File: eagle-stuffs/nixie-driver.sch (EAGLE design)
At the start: 65 parts, among them IC1 74141N/K155ID1, IC2 74LS595N, IC4 NE555, Q1 MPSA92, Q10 2N2222, Q11 IRF840, Q12 2N2222, Q2 MPSA92, Q3 MPSA92, Q4 MPSA92, Q5 MPSA42, Q6 MPSA42, Q7 MPSA42, Q8 MPSA42, Q9 PN2907, U1 MC34063DIP

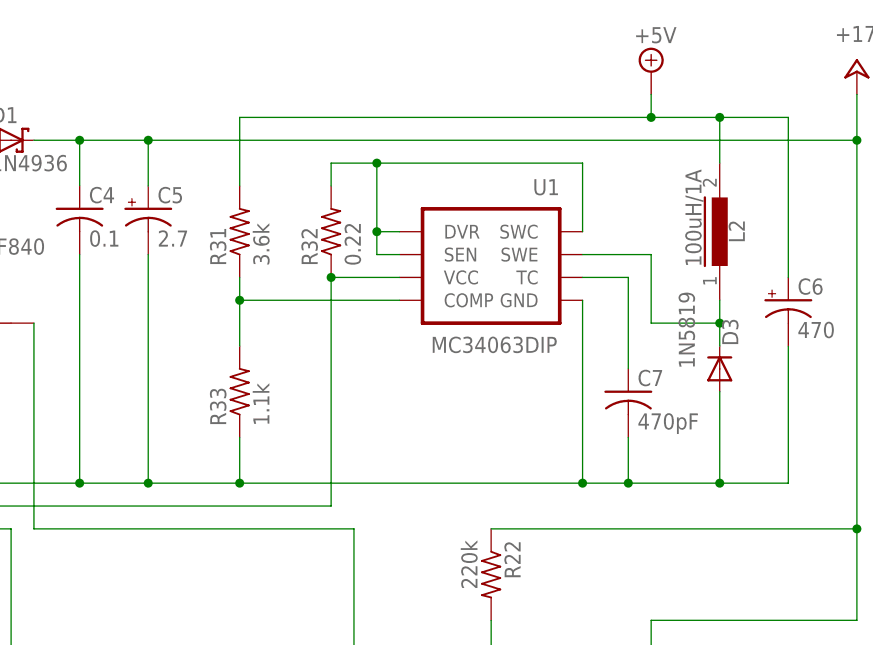
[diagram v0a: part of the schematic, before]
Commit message: Change fixed resistors for voltage output ajust. to pot.
The PI seems to be quite touchy about the voltage drop under load. Got
to push it to 5.1v to make the red led stop to blink!
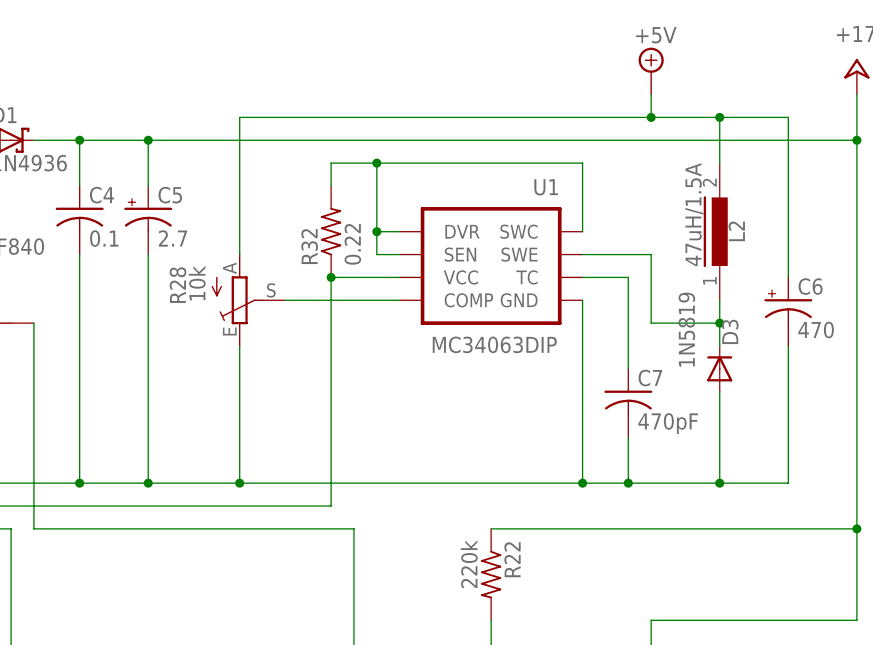
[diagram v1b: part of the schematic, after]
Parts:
- removed R31: 3.6k, resistor:R-US_0204/2V
- removed R33: 1.1k, resistor:R-US_0204/2V
- added R28: 10k, pot:TRIM_EU-CA6V
- L2: value 100uH/1A -> 47uH/1.5A
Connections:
- removed net N$67: R31.1, R33.2, U1.COMP
- new net N$61: R28.S, U1.COMP
- net +5V: now also R28.A; no longer R31.2
- net GND: now also R28.E; no longer R33.1
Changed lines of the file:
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@@
 <part name="U1" library="SparkFun-PowerIC" deviceset="MC34063" device="DIP"/>
 <part name="D3" library="diode" deviceset="1N4004" device="" value="1N5819"/>
-<part name="L2" library="inductors" deviceset="MMICC7" device="" value="100uH/1A"/>
+<part name="L2" library="inductors" deviceset="MMICC7" device="" value="47uH/1.5A"/>
 <part name="C6" library="rcl" deviceset="CPOL-US" device="E3.5-8" value="470"/>
 <part name="C7" library="rcl" deviceset="C-US" device="050-024X044" value="470pF"/>
-<part name="R31" library="resistor" deviceset="R-US_" device="0204/2V" value="3.6k"/>
 <part name="R32" library="resistor" deviceset="R-US_" device="0204/2V" value="0.22"/>
-<part name="R33" library="resistor" deviceset="R-US_" device="0204/2V" value="1.1k"/>
+<part name="R28" library="pot" deviceset="TRIM_EU-" device="CA6V" value="10k"/>
 </parts>
 <sheets>
@@
 <instance part="C6" gate="G$1" x="154.94" y="180.34"/>
 <instance part="C7" gate="G$1" x="137.16" y="170.18"/>
-<instance part="R31" gate="G$1" x="93.98" y="187.96" rot="R90"/>
 <instance part="R32" gate="G$1" x="104.14" y="187.96" rot="R90"/>
-<instance part="R33" gate="G$1" x="93.98" y="170.18" rot="R90"/>
+<instance part="R28" gate="1" x="93.98" y="180.34" rot="MR180"/>
 </instances>
 <busses>
@@
 <pinref part="Q10" gate="G$1" pin="E"/>
 <pinref part="C10" gate="G$1" pin="2"/>
-<wire x1="93.98" y1="165.1" x2="93.98" y2="160.02" width="0.1524" layer="91"/>
 <junction x="93.98" y="160.02"/>
 <pinref part="U1" gate="G$1" pin="GND"/>
@@
 <wire x1="154.94" y1="160.02" x2="154.94" y2="175.26" width="0.1524" layer="91"/>
 <junction x="147.32" y="160.02"/>
-<pinref part="R33" gate="G$1" pin="1"/>
+<pinref part="R28" gate="1" pin="E"/>
+<wire x1="93.98" y1="175.26" x2="93.98" y2="160.02" width="0.1524" layer="91"/>
 </segment>
 <segment>
@@
 <wire x1="139.7" y1="200.66" x2="139.7" y2="203.2" width="0.1524" layer="91"/>
 <wire x1="139.7" y1="200.66" x2="93.98" y2="200.66" width="0.1524" layer="91"/>
-<wire x1="93.98" y1="200.66" x2="93.98" y2="193.04" width="0.1524" layer="91"/>
 <pinref part="L2" gate="1" pin="2"/>
 <wire x1="139.7" y1="200.66" x2="147.32" y2="200.66" width="0.1524" layer="91"/>
@@
 <wire x1="154.94" y1="200.66" x2="154.94" y2="182.88" width="0.1524" layer="91"/>
 <junction x="147.32" y="200.66"/>
-<pinref part="R31" gate="G$1" pin="2"/>
+<pinref part="R28" gate="1" pin="A"/>
+<wire x1="93.98" y1="185.42" x2="93.98" y2="200.66" width="0.1524" layer="91"/>
 </segment>
 <segment>
@@
 </segment>
 </net>
-<net name="N$67" class="0">
-<segment>
-<wire x1="93.98" y1="175.26" x2="93.98" y2="180.34" width="0.1524" layer="91"/>
-<pinref part="U1" gate="G$1" pin="COMP"/>
-<wire x1="93.98" y1="180.34" x2="93.98" y2="182.88" width="0.1524" layer="91"/>
-<wire x1="111.76" y1="180.34" x2="93.98" y2="180.34" width="0.1524" layer="91"/>
-<junction x="93.98" y="180.34"/>
-<pinref part="R31" gate="G$1" pin="1"/>
-<pinref part="R33" gate="G$1" pin="2"/>
-</segment>
-</net>
 <net name="N$68" class="0">
 <segment>
@@
 </segment>
 </net>
+<net name="N$61" class="0">
+<segment>
+<pinref part="U1" gate="G$1" pin="COMP"/>
+<pinref part="R28" gate="1" pin="S"/>
+<wire x1="111.76" y1="180.34" x2="99.06" y2="180.34" width="0.1524" layer="91"/>
+</segment>
+</net>
